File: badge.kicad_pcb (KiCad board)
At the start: 2 copper layers, 99.1 x 99.1 mm, 2 parts, among them J1 Conn_01x40_Female, U1 ESP32-DEVKITC-32D

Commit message: Add btn, jumpers
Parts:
- added C1: 0.1uF, Capacitor_SMD:C_0603_1608Metric, F.Cu at (154.9, 58.4)
- added C2: 0.1uF, Capacitor_SMD:C_0603_1608Metric, F.Cu at (111.8, 83.8)
- added C3: 0.1uF, Capacitor_SMD:C_0603_1608Metric, F.Cu at (116.8, 91.4)
- added C4: 0.1uF, Capacitor_SMD:C_0603_1608Metric, F.Cu at (163.8, 91.4)
- added C5: 0.1uF, Capacitor_SMD:C_0603_1608Metric, F.Cu at (124.5, 99.1)
- added C6: 0.1uF, Capacitor_SMD:C_0603_1608Metric, F.Cu at (132.1, 91.4)
- added C7: 0.1uF, Capacitor_SMD:C_0603_1608Metric, F.Cu at (186.7, 90.2)
- added J2: DevKitC_R, Connector_PinHeader_2.54mm:PinHeader_1x20_P2.54mm_Vertical_SMD_Pin1Right, F.Cu at (153.7, 21.6)
- added J3: HT024SQV010NH, Connector_FFC-FPC:Hirose_FH12-40S-0.5SH_1x40-1MP_P0.50mm_Horizontal, B.Cu at (161.5, 66.9)
- added J4: EXT1_1, Connector_PinHeader_2.54mm:PinHeader_1x04_P2.54mm_Vertical, F.Cu at (188.0, 48.3)
- added J5: EXT1_2, Connector_PinHeader_2.54mm:PinHeader_1x04_P2.54mm_Vertical, F.Cu at (190.5, 48.3)
- added J6: EXT1_3, Connector_PinHeader_2.54mm:PinHeader_1x04_P2.54mm_Vertical, F.Cu at (193.0, 48.3)
- added J7: EXT2_1, Connector_PinHeader_2.54mm:PinHeader_1x06_P2.54mm_Vertical, F.Cu at (188.0, 61.0)
- added J8: EXT2_2, Connector_PinHeader_2.54mm:PinHeader_1x06_P2.54mm_Vertical, F.Cu at (190.5, 61.0)
- added J9: EXT2_3, Connector_PinHeader_2.54mm:PinHeader_1x06_P2.54mm_Vertical, F.Cu at (193.0, 61.0)
- added R1: 0603/12R, Resistor_SMD:R_0603_1608Metric, F.Cu at (152.7, 70.7)
- added R2: 0603/12R, Resistor_SMD:R_0603_1608Metric, F.Cu at (152.7, 73.3)
- added R3: 0603/12R, Resistor_SMD:R_0603_1608Metric, F.Cu at (152.7, 75.8)
- added SW1: UP, Button_Switch_SMD:SW_SPST_TL3342, F.Cu at (118.1, 83.8)
- added SW2: LEFT, Button_Switch_SMD:SW_SPST_TL3342, F.Cu at (110.5, 91.4)
- added SW3: A, Button_Switch_SMD:SW_SPST_TL3342, F.Cu at (170.2, 91.4)
- added SW4: DOWN, Button_Switch_SMD:SW_SPST_TL3342, F.Cu at (118.1, 99.1)
- added SW5: RIGHT, Button_Switch_SMD:SW_SPST_TL3342, F.Cu at (125.7, 91.4)
- added SW6: B, Button_Switch_SMD:SW_SPST_TL3342, F.Cu at (180.3, 90.2)
- J1: value Conn_01x40_Female -> DevKitC_L; footprint Connector_FFC-FPC:Hirose_FH12-40S-0.5SH_1x40-1MP_P0.50mm_Horizontal -> Connector_PinHeader_2.54mm:PinHeader_1x20_P2.54mm_Vertical_SMD_Pin1Right
- U1: footprint MODULE_ESP32-DEVKITC-32D -> ESP32-DEVKITC-32D:MODULE_ESP32-DEVKITC-32D
- moved U1 63.5 mm to (71.2, 33.8), turned to 270 degrees
- moved J1 57.9 mm to (153.7, 43.9)
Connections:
- net Net-(J1-Pad19) renamed +5V
- J1 pad 1: Net-(J1-Pad1) -> +3V3
- J1 pad 10: Net-(J1-Pad10) -> /GPIO26
- J1 pad 11: Net-(J1-Pad11) -> /GPIO27
- J1 pad 12: Net-(J1-Pad12) -> /GPIO14
- J1 pad 13: Net-(J1-Pad13) -> /GPIO12
- J1 pad 14: Net-(J1-Pad14) -> GND
- J1 pad 15: Net-(J1-Pad15) -> /GPIO13
- J1 pad 3: Net-(J1-Pad3) -> /GPIO36
- J1 pad 4: Net-(J1-Pad4) -> /GPIO39
- J1 pad 5: Net-(J1-Pad5) -> /GPIO34
- J1 pad 6: Net-(J1-Pad6) -> /GPIO35
- J1 pad 9: Net-(J1-Pad9) -> /GPIO25
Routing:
- net GND: track 0.00 -> 279.9 mm, vias 0 -> 6
- net /GPIO15: track 0.00 -> 131.9 mm, vias 0 -> 2
- net /GPIO4: track 0.00 -> 97.5 mm
- net /GPIO12: track 0.00 -> 68.5 mm
- net /GPIO14: track 0.00 -> 66.1 mm
- net /GPIO39: track 0.00 -> 58.5 mm, vias 0 -> 2
- net /GPIO13: track 0.00 -> 55.2 mm
- net /GPIO36: track 0.00 -> 54.7 mm, vias 0 -> 2
- net /GPIO27: track 0.00 -> 52.8 mm
- net /GPIO26: track 0.00 -> 52.5 mm
- net /GPIO25: track 0.00 -> 45.6 mm
- net +3V3: track 0.00 -> 36.9 mm
- net /GPIO35: track 0.00 -> 34.2 mm
- net /GPIO34: track 0.00 -> 26.5 mm

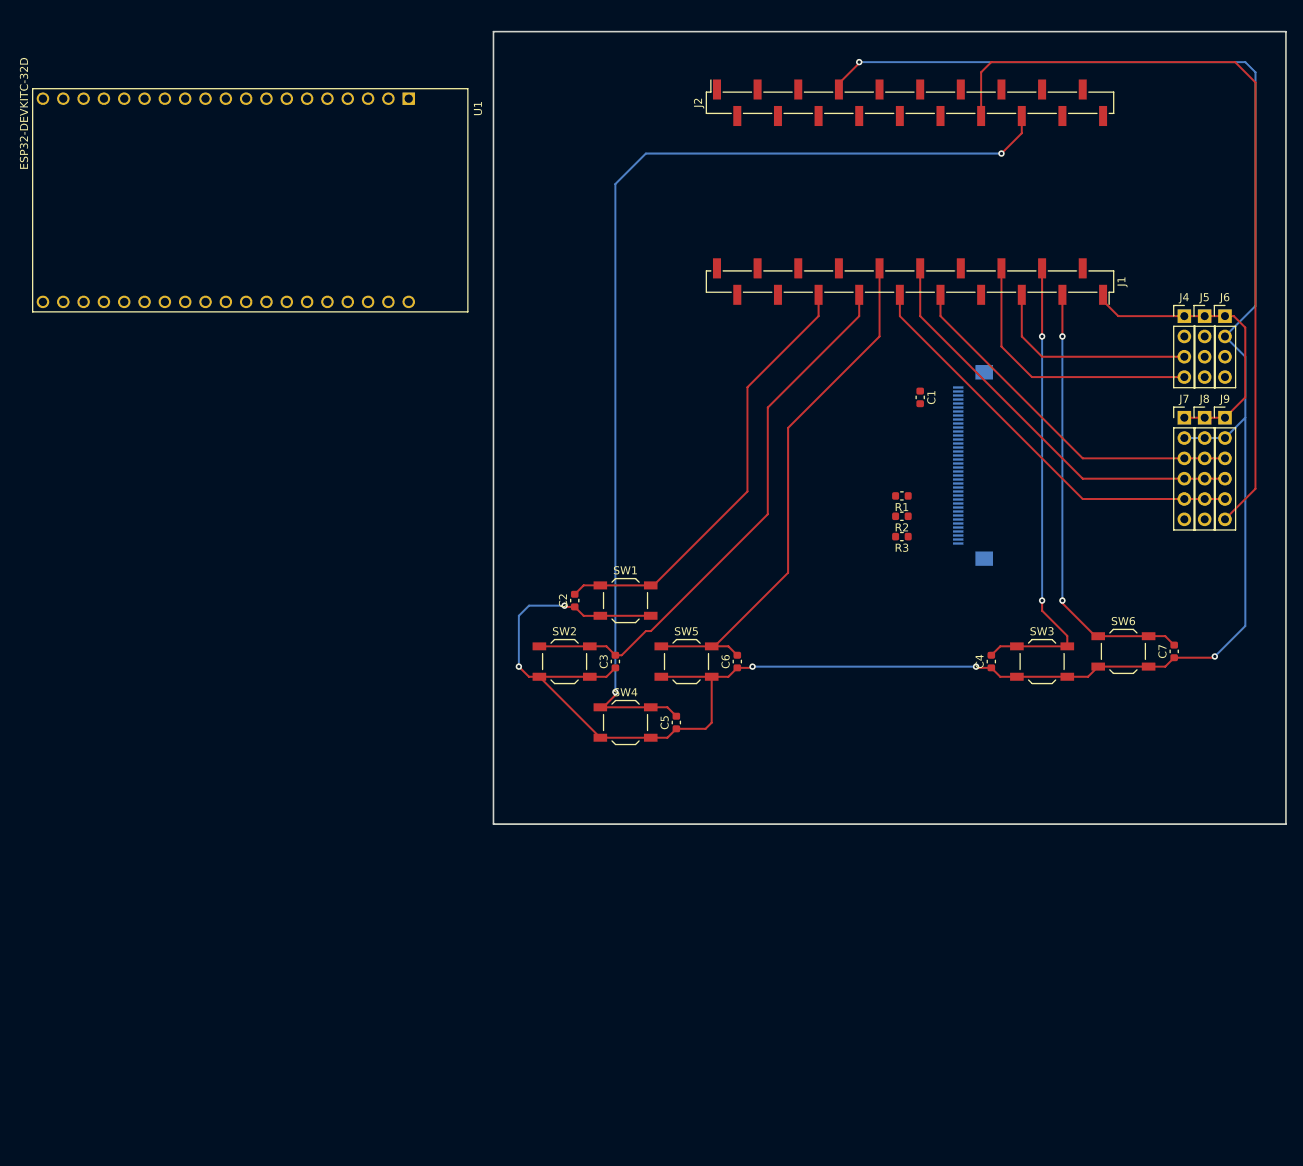
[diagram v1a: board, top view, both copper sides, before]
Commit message: Change to manual PCB
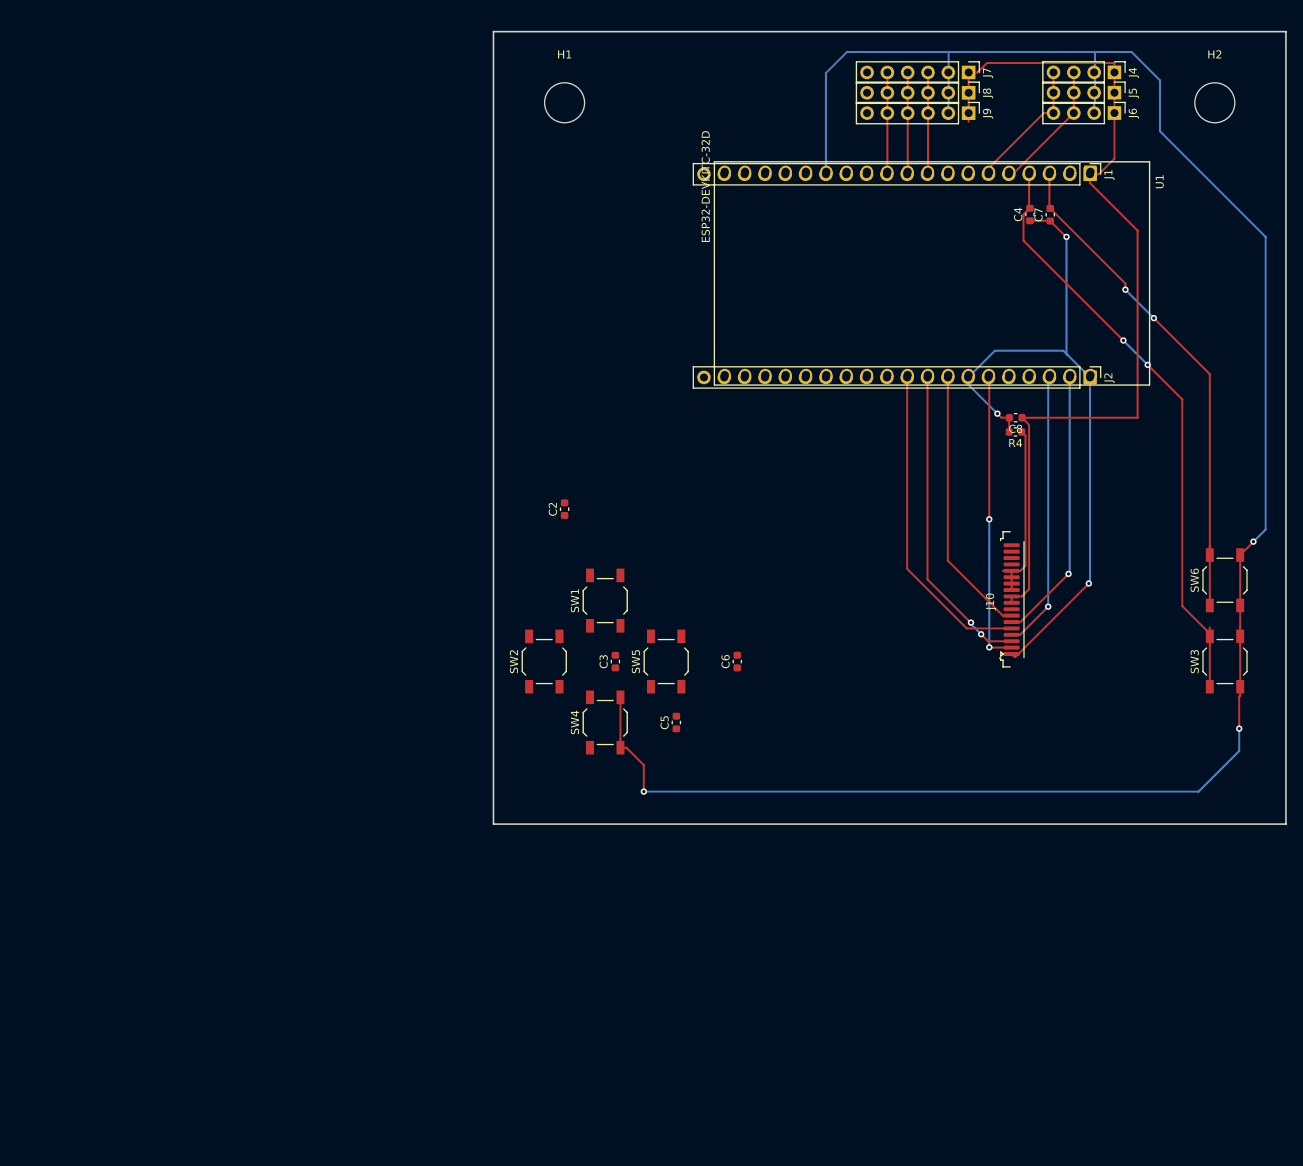
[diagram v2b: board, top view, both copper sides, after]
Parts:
- removed C1: 0.1uF, Capacitor_SMD:C_0603_1608Metric
- removed J3: HT024SQV010NH, Connector_FFC-FPC:Hirose_FH12-40S-0.5SH_1x40-1MP_P0.50mm_Horizontal
- removed R1, R2, R3: 0603/12R, Resistor_SMD:R_0603_1608Metric
- added C8: 0.1uF, Capacitor_SMD:C_0603_1608Metric, F.Cu at (166.9, 61.0)
- added H1: MountingHole, MountingHole:MountingHole_5mm, F.Cu at (110.5, 21.6)
- added H2: MountingHole, MountingHole:MountingHole_5mm, F.Cu at (191.8, 21.6)
- added J10: HT024SQV003NH, custom_footprint:COMMON_MOUNT_FFC-1x18-1MP_P0.80mm, F.Cu at (160.7, 85.4)
- added R4: 0603/4.7, Resistor_SMD:R_0603_1608Metric, F.Cu at (166.9, 62.7)
- J1, J2: footprint Connector_PinHeader_2.54mm:PinHeader_1x20_P2.54mm_Vertical_SMD_Pin1Right -> Connector_PinHeader_2.54mm:PinHeader_1x20_P2.54mm_Vertical
- moved U1 85.7 mm to (156.5, 42.9)
- moved C7 56.7 mm to (171.2, 35.6)
- moved C4 56.1 mm to (168.7, 35.6)
- moved J7 50.9 mm to (161.0, 17.8), turned to 270 degrees
- moved J8 50.2 mm to (161.0, 20.3), turned to 270 degrees
- moved J9 49.8 mm to (161.0, 22.9), turned to 270 degrees
- moved J2 41.1 mm to (176.2, 55.9), turned to 270 degrees
- moved J4 31.7 mm to (179.2, 17.8), turned to 270 degrees
- moved J5 30.1 mm to (179.2, 20.3), turned to 270 degrees
- moved J6 28.9 mm to (179.2, 22.9), turned to 270 degrees
- moved J1 26.2 mm to (176.2, 30.5)
- moved SW3 22.9 mm to (193.0, 91.4), turned to 90 degrees
- moved SW6 15.5 mm to (193.0, 81.3), turned to 90 degrees
- moved C2 11.5 mm to (110.5, 72.4)
- moved SW1 2.54 mm to (115.6, 83.8), turned to 90 degrees
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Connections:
- J2 pad 13: Net-(J2-Pad13) -> /GPIO4
- J2 pad 14: /GPIO4 -> Net-(J2-Pad14)
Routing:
- net /GPIO15: track 131.9 -> 0.00 mm, vias 2 -> 0
- net /GPIO4: track 97.5 -> 0.00 mm
- net +3V3: track 36.9 -> 113.2 mm
- net /GPIO12: track 68.5 -> 0.00 mm
- net /GPIO14: track 66.1 -> 0.00 mm
- net GND: track 279.9 -> 341.6 mm
- net /GPIO13: track 55.2 -> 0.00 mm
- net /VSPI_CS: track 0.00 -> 40.1 mm
- net /GPIO27: track 52.8 -> 12.8 mm
- net /GPIO26: track 52.5 -> 12.8 mm
- net /VSPI_SCK: track 0.00 -> 39.1 mm, vias 0 -> 2
- net /LCD_RST: track 0.00 -> 36.6 mm, vias 0 -> 2
- net /VSPI_MOSI: track 0.00 -> 35.6 mm, vias 0 -> 1
- net /LCD_DC: track 0.00 -> 34.7 mm, vias 0 -> 1
- net /VSPI_MISO: track 0.00 -> 33.7 mm
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
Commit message: Square layout
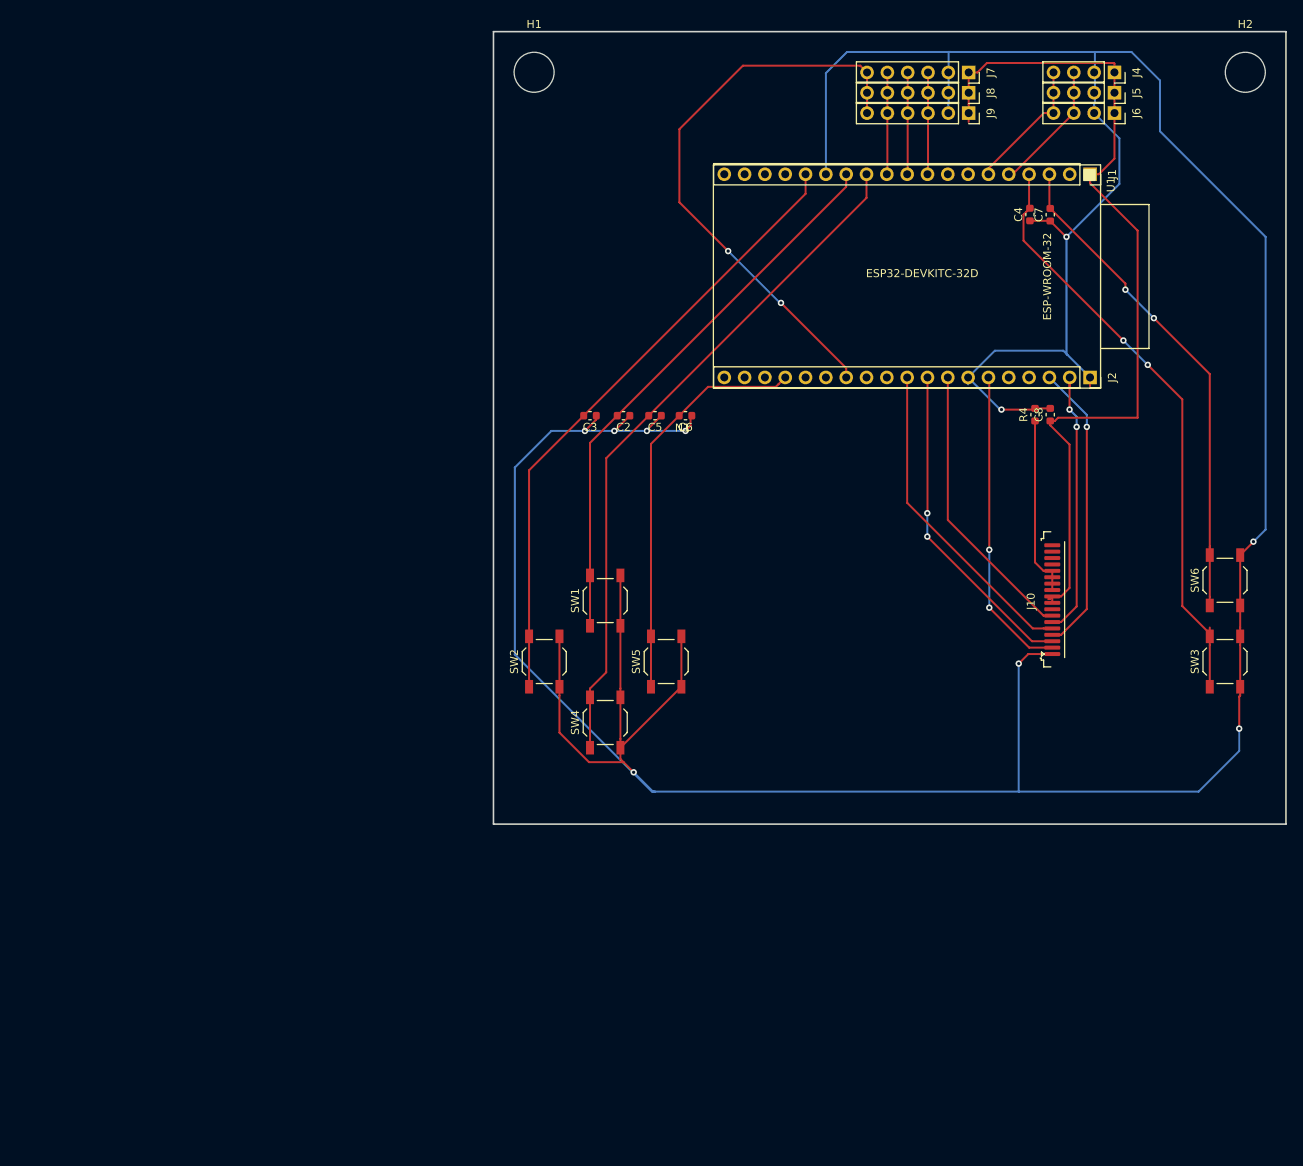
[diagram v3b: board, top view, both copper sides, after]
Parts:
- added N1: Housing, custom_footprint:2.4INCH_TFT_LCD_18P_0.80mm_FOLD, F.Cu at (127.5, 63.0)
- J1, J2: footprint Connector_PinHeader_2.54mm:PinHeader_1x20_P2.54mm_Vertical -> Connector_PinSocket_2.54mm:PinSocket_1x19_P2.54mm_Vertical
- J4, J5, J6: footprint Connector_PinHeader_2.54mm:PinHeader_1x04_P2.54mm_Vertical -> Connector_PinSocket_2.54mm:PinSocket_1x04_P2.54mm_Vertical
- J7, J8, J9: footprint Connector_PinHeader_2.54mm:PinHeader_1x06_P2.54mm_Vertical -> Connector_PinSocket_2.54mm:PinSocket_1x06_P2.54mm_Vertical
- U1: footprint ESP32-DEVKITC-32D:MODULE_ESP32-DEVKITC-32D -> custom_footprint:MODULE_ESP32-DEVKITC-32D-SILKONLY
- moved C5 38.4 mm to (121.8, 60.7), turned to 180 degrees
- moved C6 31.4 mm to (125.6, 60.7), turned to 180 degrees
- moved C3 30.9 mm to (113.7, 60.7), turned to 180 degrees
- moved C2 13.8 mm to (117.9, 60.7), turned to 180 degrees
- moved H2 5.39 mm to (195.6, 17.8)
- moved H1 5.39 mm to (106.7, 17.8)
- moved J10 5.08 mm to (165.7, 85.4)
- moved C8 4.33 mm to (171.2, 60.6), turned to 90 degrees
- moved R4 3.26 mm to (169.3, 60.6), turned to 90 degrees
- moved U1 0.40 mm to (156.3, 43.3)
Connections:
- C2 pad 2: /GPIO13 -> /GPIO12
- C3 pad 2: /GPIO12 -> /GPIO13
- C5 pad 2: /GPIO15 -> /GPIO14
- C6 pad 2: /GPIO14 -> /GPIO15
- SW1 pad 1: /GPIO13 -> /GPIO12
- SW2 pad 1: /GPIO12 -> /GPIO13
- SW4 pad 1: /GPIO15 -> /GPIO14
- SW5 pad 1: /GPIO14 -> /GPIO15
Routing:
- net GND: track 341.6 -> 479.6 mm, vias 6 -> 10
- net /GPIO14: track 0.00 -> 86.0 mm
- net /GPIO13: track 0.00 -> 78.4 mm
- net /GPIO4: track 0.00 -> 71.9 mm, vias 0 -> 2
- net /GPIO12: track 0.00 -> 69.7 mm
- net /GPIO15: track 0.00 -> 50.6 mm
- net +3V3: track 113.2 -> 110.6 mm
- net /LCD_RST: track 36.6 -> 38.8 mm
- net /VSPI_MISO: track 33.7 -> 35.8 mm
- net /LCD_DC: track 34.7 -> 36.8 mm
- net /VSPI_SCK: track 39.1 -> 40.9 mm
- net /VSPI_MOSI: track 35.6 -> 34.1 mm, vias 1 -> 2

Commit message: Arranged to v0.1
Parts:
- added D1: 0603/BLUE, LED_SMD:LED_0603_1608Metric, F.Cu at (148.8, 60.5)
- added D2: 0603/RED, LED_SMD:LED_0603_1608Metric, F.Cu at (150.6, 60.5)
- added H3: MountingHole, MountingHole:MountingHole_8.4mm_M8, F.Cu at (119.4, 40.6)
- added H4: MountingHole, MountingHole:MountingHole_8.4mm_M8, F.Cu at (119.4, 38.1)
- added R5: 0603/470R, Resistor_SMD:R_0603_1608Metric, F.Cu at (147.1, 60.5)
- added R6: 0603/1K, Resistor_SMD:R_0603_1608Metric, F.Cu at (145.3, 60.5)
- J4, J5, J6: footprint Connector_PinSocket_2.54mm:PinSocket_1x04_P2.54mm_Vertical -> custom_footprint:PinSocket_1x04_P2.54mm_Vertical_NO3D
- J7, J8, J9: footprint Connector_PinSocket_2.54mm:PinSocket_1x06_P2.54mm_Vertical -> custom_footprint:PinSocket_1x06_P2.54mm_Vertical_NO3D
- N1: value Housing -> 2.4" LCD
- R4: value 0603/4.7 -> 0603/4.7R
- moved C2 37.8 mm to (145.7, 35.2), turned to 90 degrees
- moved C3 37.1 mm to (140.6, 35.2), turned to 90 degrees
- moved C5 36.7 mm to (148.2, 35.2), turned to 270 degrees
- moved C6 12.6 mm to (138.2, 60.5), turned to 90 degrees
- moved SW4 8.90 mm to (116.1, 90.2), turned to 270 degrees
- moved SW2 7.73 mm to (109.2, 83.8), turned to 270 degrees
- moved SW5 7.69 mm to (122.9, 83.8)
- moved SW1 6.37 mm to (116.1, 77.5)
- moved SW6 3.97 mm to (196.1, 78.7)
- moved SW3 3.64 mm to (192.3, 87.9)
- moved C7 0.28 mm to (171.2, 35.3)
- moved C4 0.25 mm to (168.7, 35.3)
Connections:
- net Net-(J1-Pad7) renamed /GPIO32
- J2 pad 11: Net-(J2-Pad11) -> /GPIO17
- J2 pad 12: Net-(J2-Pad12) -> /GPIO16
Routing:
- net /GPIO13: track 78.4 -> 68.7 mm
- net /GPIO14: track 86.0 -> 77.8 mm
- net Net-(D2-Pad2): track 0.00 -> 6.58 mm
- net /GPIO12: track 69.7 -> 63.1 mm
- net +3V3: track 110.6 -> 104.3 mm
- net /GPIO15: track 50.6 -> 45.9 mm
- net GND: track 479.6 -> 484.2 mm
- net /GPIO16: track 0.00 -> 3.99 mm
- net /GPIO39: track 75.2 -> 71.3 mm
- net /GPIO17: track 0.00 -> 3.80 mm
- net /GPIO36: track 63.5 -> 67.2 mm
- net Net-(D1-Pad2): track 0.00 -> 1.78 mm
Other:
- outline, holes or cut-outs redrawn
